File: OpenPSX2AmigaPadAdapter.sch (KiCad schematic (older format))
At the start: 36 parts, among them J1 TO_PSX_PAD, J2 DB9_F, J3 CONN_FTDI, J4 CONN_ICSP, J99 OSHW_LOGO, Q1 BSS138, Q2 BSS138, Q3 BSS138, Q4 BSS138, SW1 RESET, U1 ATmega328P-AU, U2 LM1117-3.3, Y1 16MHz

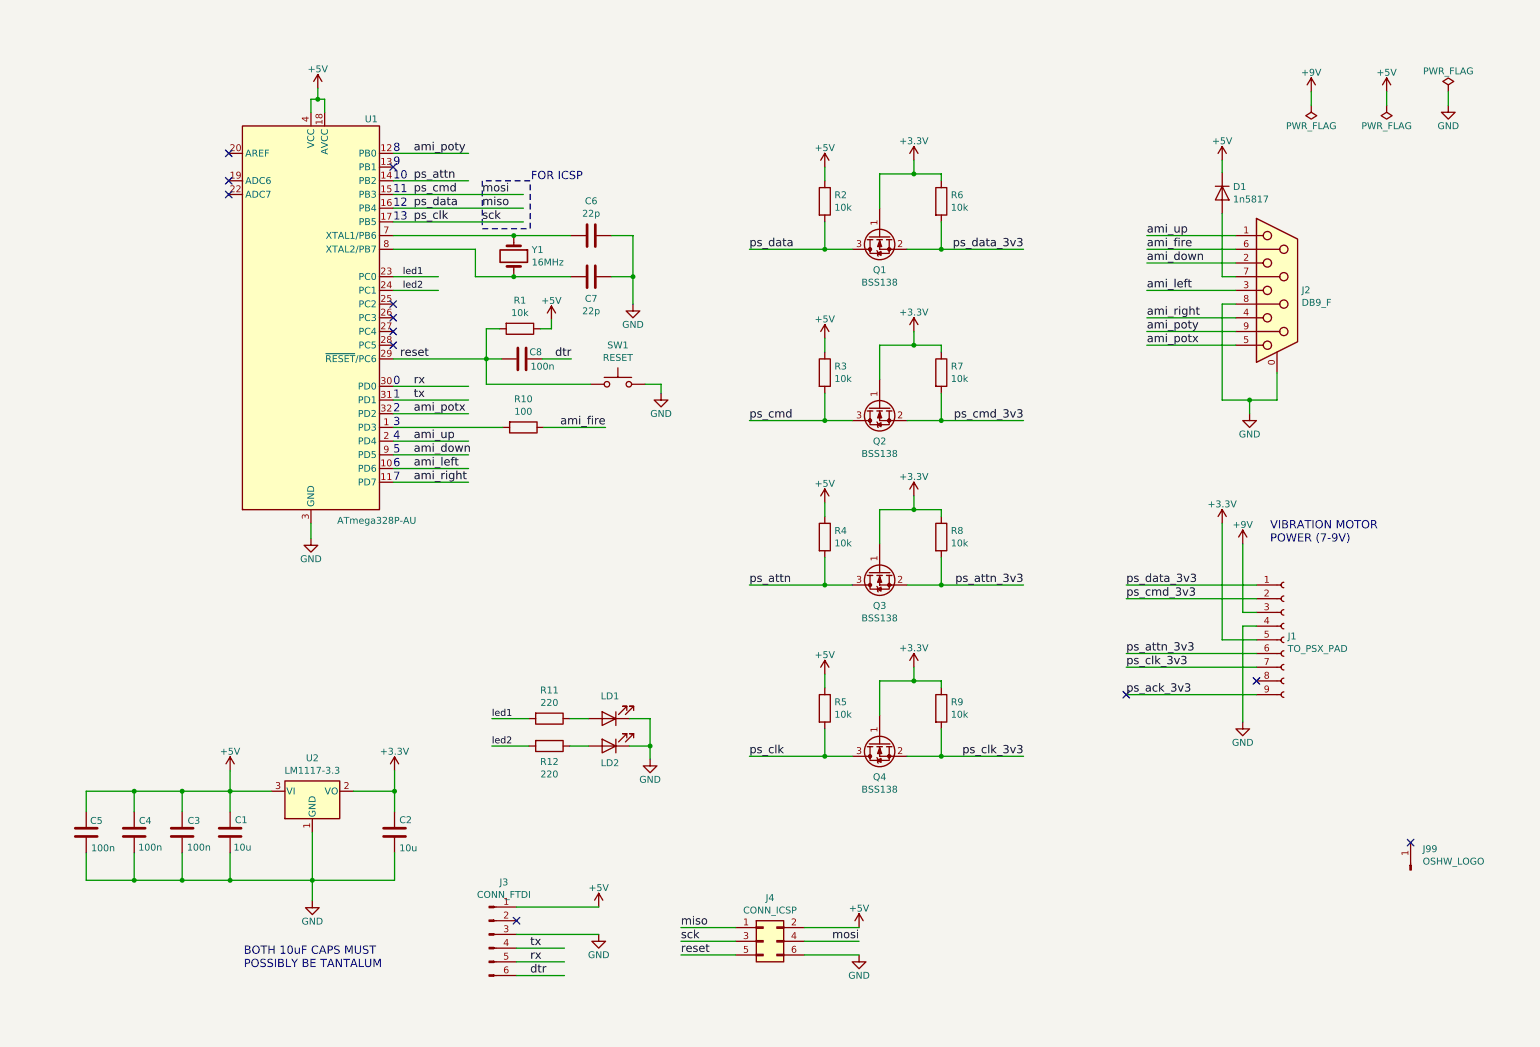
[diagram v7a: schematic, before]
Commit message: Add pull-up resistors on DATA and ACK
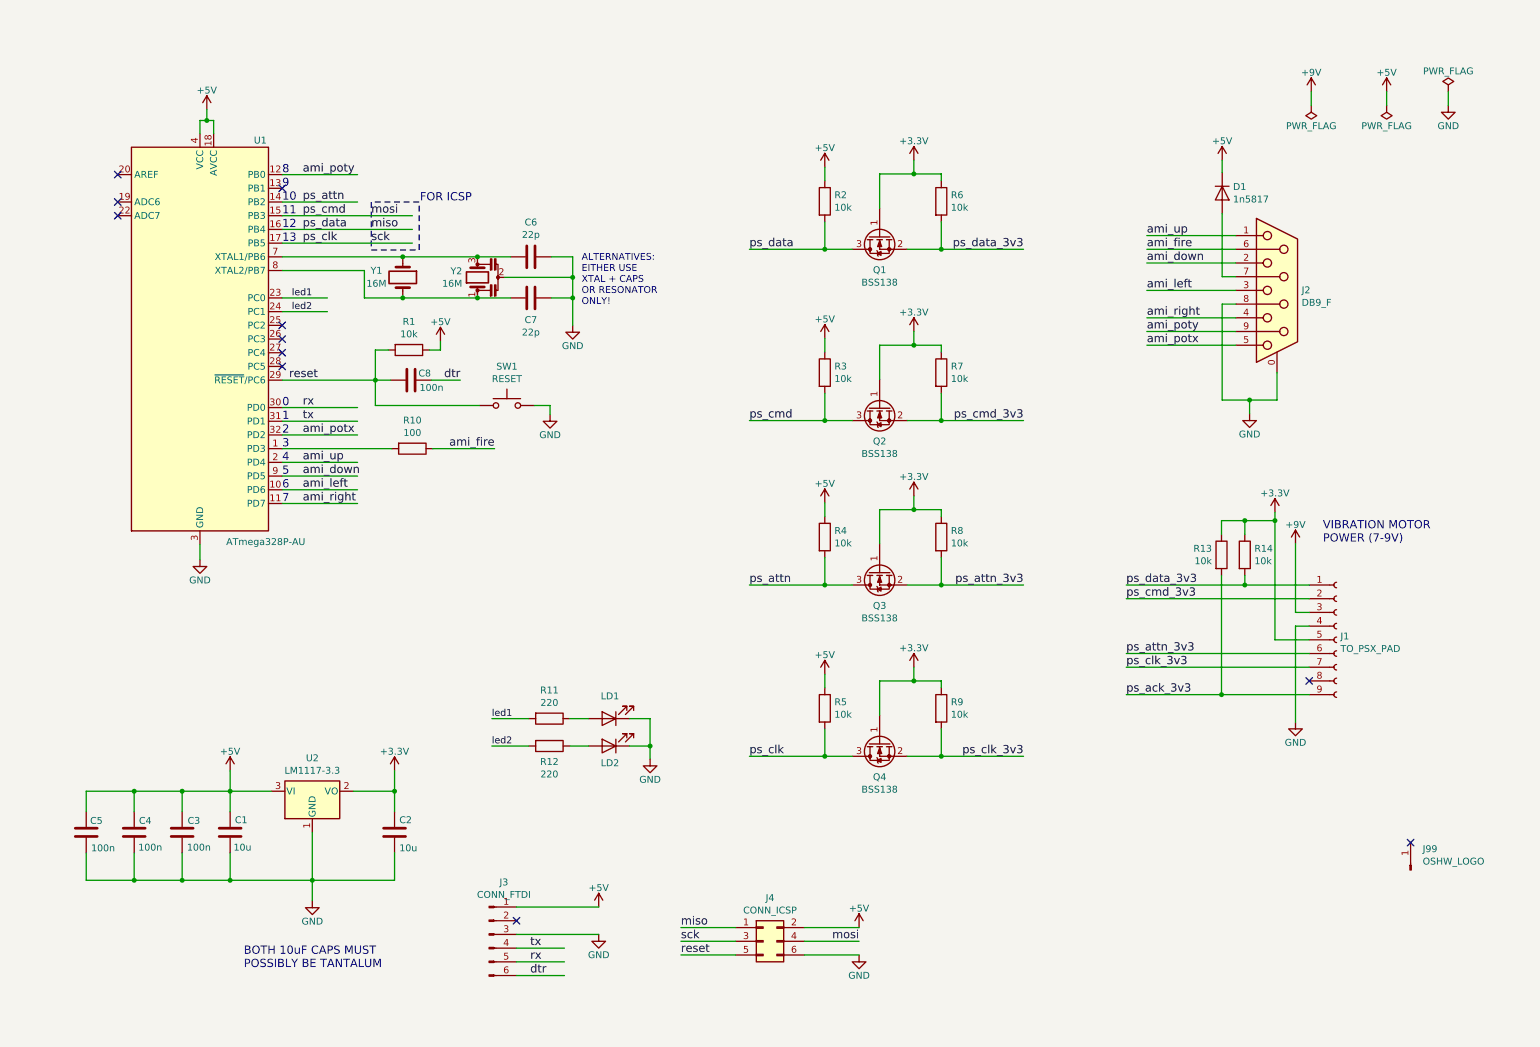
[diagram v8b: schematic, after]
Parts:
- added R13, R14: 10k, Resistor_SMD:R_0805_2012Metric_Pad1.15x1.40mm_HandSolder, symbol Device:R
- added Y2: 16M, Crystal:Resonator_SMD_muRata_CSTxExxV-3Pin_3.0x1.1mm, symbol Device:Resonator
- Y1: value 16MHz -> 16M
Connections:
- wire segments 164 -> 177
- no-connect marks 12 -> 11
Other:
- note added: "ALTERNATIVES:\nEITHER USE\nXTAL + CAPS\nOR RESONATOR\nONLY!"
- moved on the sheet: C6, C7, C8, J1, R1, R10, SW1, U1, Y1
